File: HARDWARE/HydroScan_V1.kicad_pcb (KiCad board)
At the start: 4 copper layers, 202 x 100 mm, 0 parts

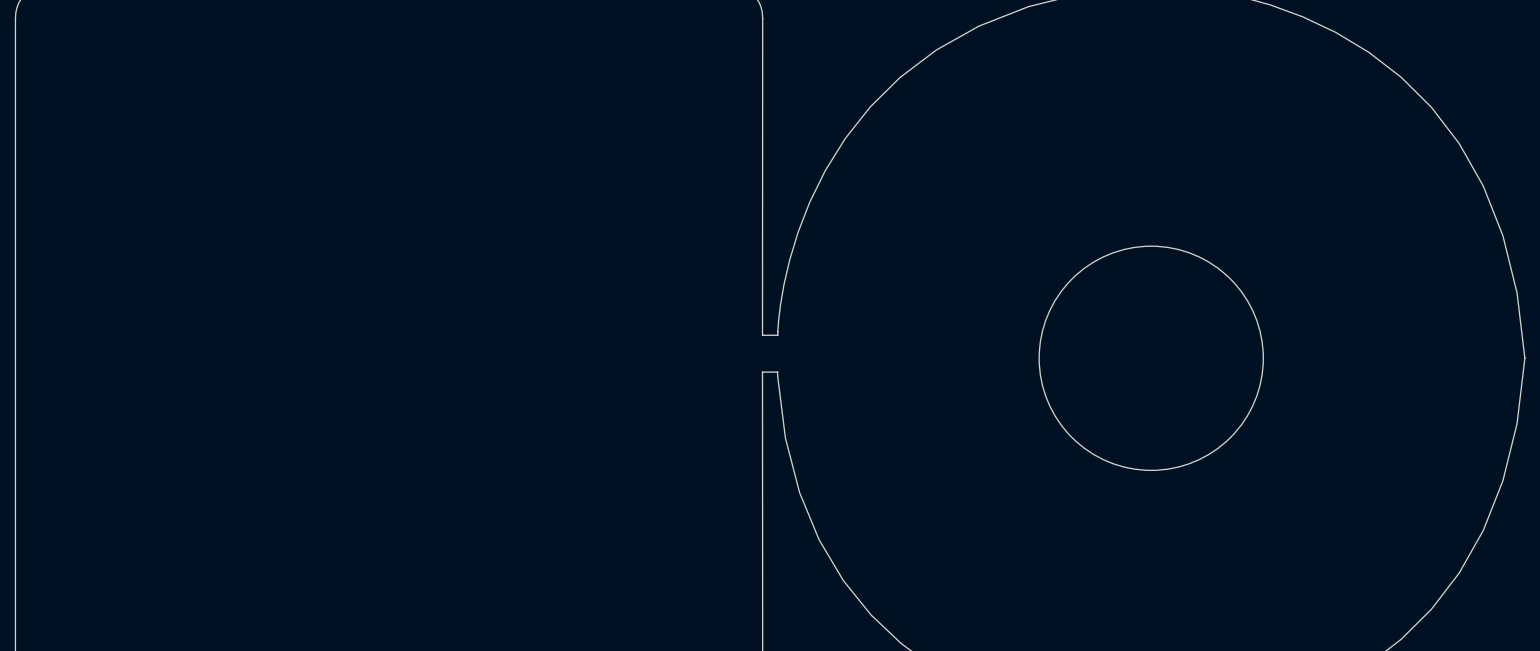
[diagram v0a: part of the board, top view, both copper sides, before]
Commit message: Integrate ESP32
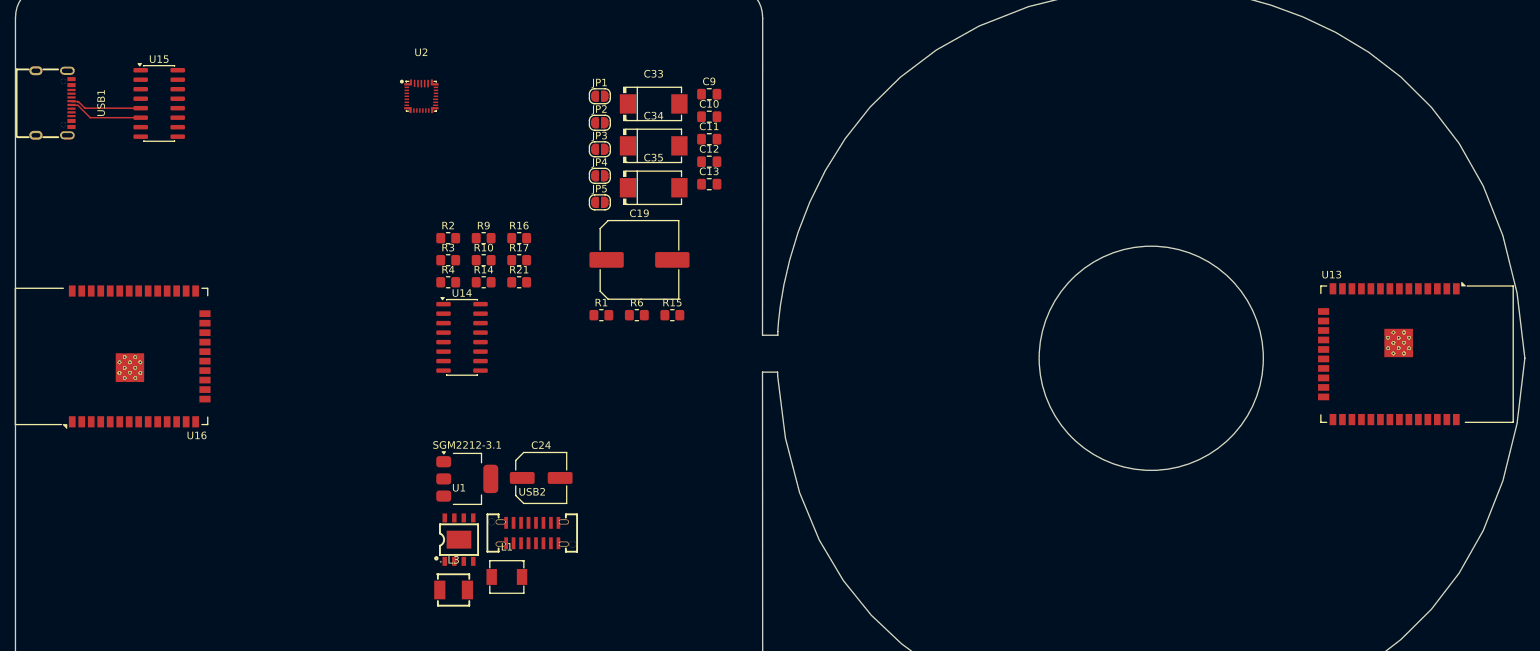
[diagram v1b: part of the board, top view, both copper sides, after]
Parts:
- added C10: 22uf, Capacitor_SMD:C_0805_2012Metric_Pad1.18x1.45mm_HandSolder, F.Cu at (172.8, 137.7)
- added C11: 10uf, Capacitor_SMD:C_0805_2012Metric_Pad1.18x1.45mm_HandSolder, F.Cu at (172.8, 140.7)
- added C12: 22uf, Capacitor_SMD:C_0805_2012Metric_Pad1.18x1.45mm_HandSolder, F.Cu at (172.8, 143.7)
- added C13: 22uf, Capacitor_SMD:C_0805_2012Metric_Pad1.18x1.45mm_HandSolder, F.Cu at (172.8, 146.7)
- added C19: 470uf, Capacitor_SMD:C_Elec_10x10.2, F.Cu at (163.5, 156.8)
- added C24: 47uf, Capacitor_SMD:C_Elec_6.3x7.7, F.Cu at (150.4, 186.0)
- added C33: 25TQC33MYF, EasyEDA:CAP-SMD_L7.3-W4.3-FD, F.Cu at (165.4, 136.0)
- added C34: 25TQC33MYF, EasyEDA:CAP-SMD_L7.3-W4.3-FD, F.Cu at (165.4, 141.6)
- added C35: 25TQC33MYF, EasyEDA:CAP-SMD_L7.3-W4.3-FD, F.Cu at (165.4, 147.2)
- added C9: 10uf, Capacitor_SMD:C_0805_2012Metric_Pad1.18x1.45mm_HandSolder, F.Cu at (172.8, 134.7)
- added JP1: SolderJumper_2_Open, Jumper:SolderJumper-2_P1.3mm_Open_RoundedPad1.0x1.5mm, F.Cu at (158.2, 134.9)
- added JP2: SolderJumper_2_Open, Jumper:SolderJumper-2_P1.3mm_Open_RoundedPad1.0x1.5mm, F.Cu at (158.2, 138.5)
- added JP3: SolderJumper_2_Open, Jumper:SolderJumper-2_P1.3mm_Open_RoundedPad1.0x1.5mm, F.Cu at (158.2, 142.0)
- added JP4: SolderJumper_2_Open, Jumper:SolderJumper-2_P1.3mm_Open_RoundedPad1.0x1.5mm, F.Cu at (158.2, 145.6)
- added JP5: SolderJumper_2_Open, Jumper:SolderJumper-2_P1.3mm_Open_RoundedPad1.0x1.5mm, F.Cu at (158.2, 149.1)
- added L1: APH0420T1R0M, EasyEDA:IND-SMD_L4.4-W4.2, F.Cu at (145.8, 199.3)
- added L3: 0420CDMCCDS-1R0MC, EasyEDA:IND-SMD_L4.2-W4.2_MCW-0420, F.Cu at (138.6, 201.0)
- added R1: 2R, Resistor_SMD:R_0805_2012Metric_Pad1.20x1.40mm_HandSolder, F.Cu at (158.4, 164.2)
- added R10: 0.5R, Resistor_SMD:R_0805_2012Metric_Pad1.20x1.40mm_HandSolder, F.Cu at (142.7, 156.9)
- added R14: 2.2k, Resistor_SMD:R_0805_2012Metric_Pad1.20x1.40mm_HandSolder, F.Cu at (142.7, 159.8)
- added R15: 2.2k, Resistor_SMD:R_0805_2012Metric_Pad1.20x1.40mm_HandSolder, F.Cu at (167.9, 164.2)
- added R16: 2.2k, Resistor_SMD:R_0805_2012Metric_Pad1.20x1.40mm_HandSolder, F.Cu at (147.4, 153.9)
- added R17: 2.2k, Resistor_SMD:R_0805_2012Metric_Pad1.20x1.40mm_HandSolder, F.Cu at (147.4, 156.9)
- added R2: 51k, Resistor_SMD:R_0805_2012Metric_Pad1.20x1.40mm_HandSolder, F.Cu at (137.9, 153.9)
- added R21: 100, Resistor_SMD:R_0805_2012Metric_Pad1.20x1.40mm_HandSolder, F.Cu at (147.4, 159.8)
- added R3: 100, Resistor_SMD:R_0805_2012Metric_Pad1.20x1.40mm_HandSolder, F.Cu at (137.9, 156.9)
- added R4: 100, Resistor_SMD:R_0805_2012Metric_Pad1.20x1.40mm_HandSolder, F.Cu at (137.9, 159.8)
- added R6: 2.2k, Resistor_SMD:R_0805_2012Metric_Pad1.20x1.40mm_HandSolder, F.Cu at (163.2, 164.2)
- added R9: 1k, Resistor_SMD:R_0805_2012Metric_Pad1.20x1.40mm_HandSolder, F.Cu at (142.7, 153.9)
- added SGM2212-3.1: ~, Package_TO_SOT_SMD:SOT-223, F.Cu at (140.5, 186.1)
- added U1: IP2312-4V35, EasyEDA:ESOP-8_L4.9-W3.9-P1.27-LS6.0-BL-EP, F.Cu at (139.4, 194.3)
- added U13: ESP32-WROOM-32D, RF_Module:ESP32-WROOM-32D, F.Cu at (264.6, 169.4)
- added U14: CH340C, Package_SO:SOIC-16_3.9x9.9mm_P1.27mm, F.Cu at (139.8, 167.2)
- added U15: CH340C, Package_SO:SOIC-16_3.9x9.9mm_P1.27mm, F.Cu at (99.2, 135.9)
- added U16: ESP32-WROOM-32D, RF_Module:ESP32-WROOM-32D, F.Cu at (95.8, 169.8)
- added U2: BQ25798RQMR, EasyEDA:QFN-29_L4.0-W4.0-P0.40-TL-BQ25792RQMR, F.Cu at (134.3, 135.0)
- added USB1: TYPE-C 16PIN 2MD, EasyEDA:USB-C-SMD_TYPE-C-16PIN-2MD-073, F.Cu at (85.1, 135.8)
- added USB2: HX-TYPE-C 16P 180 LT H15.0, EasyEDA:USB-C-SMD_HX-TYPE-C-16P-180-LT-H15.0, F.Cu at (149.2, 193.4)
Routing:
- net /Data-_1: track 0.00 -> 9.98 mm
- net /Data+_1: track 0.00 -> 9.71 mm
- added copper zone on In1.Cu, net GND

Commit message: Aclaracion de avances
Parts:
- moved U2 33.9 mm to (141.8, 168.0)
- moved C19 17.6 mm to (152.0, 170.1)
- moved U1 7.60 mm to (132.2, 191.8)
- moved C24 7.60 mm to (143.2, 183.6)
- moved C33 7.60 mm to (158.2, 133.5)
- moved C34 7.60 mm to (158.2, 139.1)
- moved C35 7.60 mm to (158.2, 144.7)
- moved JP1 7.60 mm to (151.0, 132.5)
- moved JP2 7.60 mm to (151.0, 136.0)
- moved JP3 7.60 mm to (151.0, 139.6)
- moved JP4 7.60 mm to (151.0, 143.1)
- moved JP5 7.60 mm to (151.0, 146.7)
- moved L3 7.60 mm to (131.4, 198.5)
- moved R1 7.60 mm to (151.2, 161.8)
- moved R10 7.60 mm to (135.5, 154.4)
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
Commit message: Avances puerto USB C
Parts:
- added C22: 0.1uf, Capacitor_SMD:C_0805_2012Metric_Pad1.18x1.45mm_HandSolder, F.Cu at (175.3, 142.9)
- added C23: 0.1uf, Capacitor_SMD:C_0805_2012Metric_Pad1.18x1.45mm_HandSolder, F.Cu at (175.3, 160.5)
- added D1: SM05.TCT, EasyEDA:SOT-23-3_L2.9-W1.3-P0.95-LS2.4-BR, F.Cu at (169.2, 154.6)
- added D27: LESD5D5.0CT1G, EasyEDA:SOD-523_L1.2-W0.8-LS1.6-BI, F.Cu at (145.9, 152.9)
- added D28: LESD5D5.0CT1G, EasyEDA:SOD-523_L1.2-W0.8-LS1.6-BI, F.Cu at (145.9, 155.1)
- added D29: LESD5D5.0CT1G, EasyEDA:SOD-523_L1.2-W0.8-LS1.6-BI, F.Cu at (145.9, 157.2)
- added D30: LESD5D5.0CT1G, EasyEDA:SOD-523_L1.2-W0.8-LS1.6-BI, F.Cu at (145.9, 159.3)
- added D31: LESD5D5.0CT1G, EasyEDA:SOD-523_L1.2-W0.8-LS1.6-BI, F.Cu at (145.9, 161.5)
- added D33: LESD5D5.0CT1G, EasyEDA:SOD-523_L1.2-W0.8-LS1.6-BI, F.Cu at (145.9, 163.6)
- added D4: SM05.TCT, EasyEDA:SOT-23-3_L2.9-W1.3-P0.95-LS2.4-BR, F.Cu at (169.5, 148.9)
- added R84: 1M, Capacitor_SMD:C_0805_2012Metric_Pad1.18x1.45mm_HandSolder, F.Cu at (175.3, 144.9)
- added R85: 1M, Capacitor_SMD:C_0805_2012Metric_Pad1.18x1.45mm_HandSolder, F.Cu at (175.3, 158.4)
- moved C24 122.2 mm to (164.8, 63.2)
- moved R14 122.2 mm to (157.1, 37.0)
- moved R21 122.2 mm to (161.8, 37.0)
- moved R4 122.2 mm to (152.3, 37.0)
- moved SGM2212-3.1 122.2 mm to (154.8, 63.4)
- moved U14 122.2 mm to (154.2, 44.4)
- moved C11 122.2 mm to (194.4, 20.4)
- moved C33 122.2 mm to (179.8, 13.2)
- moved C35 122.2 mm to (179.8, 24.4)
- moved JP1 122.2 mm to (172.6, 12.1)
- moved JP4 122.2 mm to (172.6, 22.8)
- moved L1 122.2 mm to (160.2, 76.5)
- moved R16 122.2 mm to (161.8, 31.1)
- moved R2 122.2 mm to (152.3, 31.1)
- moved R9 122.2 mm to (157.1, 31.1)
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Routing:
- net /V5_1: track 0.00 -> 12.8 mm
- net Net-(C22-Pad1): track 0.00 -> 9.76 mm, vias 0 -> 1
- net Net-(C23-Pad1): track 0.00 -> 9.12 mm, vias 0 -> 1
- net GND: track 0.00 -> 5.07 mm, vias 0 -> 7
- net /Data+_1: track 9.71 -> 14.7 mm
- net /Data-_1: track 9.98 -> 14.6 mm, vias 0 -> 2
- net /CC1_1: track 0.00 -> 3.02 mm
- net /CC2_1: track 0.00 -> 2.01 mm

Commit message: Avances v1
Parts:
- removed D33: LESD5D5.0CT1G, EasyEDA:SOD-523_L1.2-W0.8-LS1.6-BI
- added D22: 1N5819HW-7-F, EasyEDA:SOD-123_L2.7-W1.6-LS3.7-RD, F.Cu at (179.8, 67.8)
- added D5: SS54_C22452, EasyEDA:SMA_L4.4-W2.8-LS5.4-R-RD, F.Cu at (169.8, 162.6)
- added R13: 5.11k, Capacitor_SMD:C_0805_2012Metric_Pad1.18x1.45mm_HandSolder, F.Cu at (169.8, 145.4)
- added R83: 5.11k, Capacitor_SMD:C_0805_2012Metric_Pad1.18x1.45mm_HandSolder, F.Cu at (169.8, 157.6)
- moved D27 121.6 mm to (206.8, 47.7)
- moved D29 121.6 mm to (206.8, 52.0)
- moved D30 121.6 mm to (206.8, 54.1)
- moved D31 121.6 mm to (206.8, 56.2)
- moved D28 121.6 mm to (206.8, 49.9)
- moved U2 1.58 mm to (161.8, 177.7)
- moved D4 0.90 mm to (169.0, 148.2)
- moved D1 0.30 mm to (169.0, 154.4)
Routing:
- net /V5_1: track 12.8 -> 21.8 mm, vias 0 -> 20
- net GND: track 5.07 -> 11.8 mm, vias 7 -> 34
- net /CC2_1: track 2.01 -> 8.42 mm
- net /CC1_1: track 3.02 -> 8.38 mm
- added copper zone on In2.Cu, net /V5_1
- added copper zone on B.Cu, net GND
- added copper zone on F.Cu, net GND

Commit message: EsP32 terminate
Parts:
- added BOOT1: BOOT, EasyEDA:SW-SMD_4P-L6.0-W6.0-P4.50-LS8.2, F.Cu at (191.2, 85.1)
- added C1: 10uf_25v, Capacitor_SMD:C_0805_2012Metric_Pad1.18x1.45mm_HandSolder, F.Cu at (214.0, 87.8)
- added C14: 0.1uf, Capacitor_SMD:C_0805_2012Metric_Pad1.18x1.45mm_HandSolder, F.Cu at (126.1, 149.3)
- added C15: 0.1uf, Capacitor_SMD:C_0805_2012Metric_Pad1.18x1.45mm_HandSolder, F.Cu at (139.1, 149.3)
- added C16: 100nf, Capacitor_SMD:C_0805_2012Metric_Pad1.18x1.45mm_HandSolder, F.Cu at (118.3, 129.0)
- added C17: 10uf_25v, Capacitor_SMD:C_0805_2012Metric_Pad1.18x1.45mm_HandSolder, F.Cu at (118.3, 131.0)
- added C18: 100nf, Capacitor_SMD:C_0805_2012Metric_Pad1.18x1.45mm_HandSolder, F.Cu at (166.0, 160.0)
- added C2: 0.1uf_50v, Capacitor_SMD:C_0805_2012Metric_Pad1.18x1.45mm_HandSolder, F.Cu at (214.0, 90.9)
- added C20: 0.1uf, Capacitor_SMD:C_0805_2012Metric_Pad1.18x1.45mm_HandSolder, F.Cu at (136.3, 182.5)
- added C21: 10uf, Capacitor_SMD:C_0805_2012Metric_Pad1.18x1.45mm_HandSolder, F.Cu at (223.6, 93.9)
- added C27: 47nf, Capacitor_SMD:C_0805_2012Metric, B.Cu at (146.2, 186.2)
- added C28: 47nf, Capacitor_SMD:C_0805_2012Metric, B.Cu at (149.4, 186.2)
- added C3: 0.1uf_50v, Capacitor_SMD:C_0805_2012Metric_Pad1.18x1.45mm_HandSolder, F.Cu at (214.0, 93.9)
- added C39: 100nf, Capacitor_SMD:C_0805_2012Metric_Pad1.18x1.45mm_HandSolder, F.Cu at (164.0, 137.8)
- added C4: 10uf_25v, Capacitor_SMD:C_0805_2012Metric_Pad1.18x1.45mm_HandSolder, F.Cu at (214.0, 96.9)
- added C40: 100nf, Capacitor_SMD:C_0805_2012Metric_Pad1.18x1.45mm_HandSolder, F.Cu at (154.8, 143.4)
- added C5: 100nf, Capacitor_SMD:C_0805_2012Metric_Pad1.18x1.45mm_HandSolder, F.Cu at (214.0, 99.9)
- added C51: CL32B106KBJNNNE, EasyEDA:C1210, F.Cu at (130.3, 183.1)
- added C52: CL32B106KBJNNNE, EasyEDA:C1210, F.Cu at (133.6, 183.1)
- added C6: 10uf_25v, Capacitor_SMD:C_0805_2012Metric_Pad1.18x1.45mm_HandSolder, F.Cu at (218.8, 87.8)
- added C7: 0.1uf, Capacitor_SMD:C_0805_2012Metric_Pad1.18x1.45mm_HandSolder, F.Cu at (218.8, 90.9)
- added C8: 0.1uf, Capacitor_SMD:C_0805_2012Metric_Pad1.18x1.45mm_HandSolder, F.Cu at (218.8, 93.9)
- added CN2: DB128V-5.08-2P-GN-S, EasyEDA:CONN-TH_2P-P5.08_DIBO_DB128V-5.08, F.Cu at (161.0, 214.1)
- added L2: PSPMAA0805-101M-ANP, EasyEDA:IND-SMD_L8.5-W8.0_PCC-M0854M, F.Cu at (168.6, 153.7)
- added LED10: YLED0805G, EasyEDA:LED0805-FD-GREEN, F.Cu at (232.0, 94.9)
- added LED11: YLED0805G, EasyEDA:LED0805-FD-GREEN, F.Cu at (232.0, 98.2)
- added LED12: YLED0805G, EasyEDA:LED0805-FD-GREEN, F.Cu at (232.0, 101.5)
- added LED13: YLED0805G, EasyEDA:LED0805-FD-GREEN, F.Cu at (232.0, 104.8)
- added LED14: YLED0805G, EasyEDA:LED0805-FD-GREEN, F.Cu at (232.0, 108.1)
- added LED15: YLED0805G, EasyEDA:LED0805-FD-GREEN, F.Cu at (232.0, 111.4)
- added LED16: YLED0805G, EasyEDA:LED0805-FD-GREEN, F.Cu at (175.7, 146.6)
- added LED17: YLED0805G, EasyEDA:LED0805-FD-GREEN, F.Cu at (175.6, 149.0)
- added LED9: YLED0805G, EasyEDA:LED0805-FD-GREEN, F.Cu at (232.0, 91.6)
- added Q13: 2n3904S-RTK/PS_C18536, EasyEDA:SOT-23-3_L2.9-W1.3-P1.90-LS2.4-TR, F.Cu at (174.9, 115.7)
- added Q14: 2n3904S-RTK/PS_C18536, EasyEDA:SOT-23-3_L2.9-W1.3-P1.90-LS2.4-TR, F.Cu at (146.1, 138.1)
- added Q15: 2n3904S-RTK/PS_C18536, EasyEDA:SOT-23-3_L2.9-W1.3-P1.90-LS2.4-TR, F.Cu at (175.5, 98.8)
- added Q16: 2n3904S-RTK/PS_C18536, EasyEDA:SOT-23-3_L2.9-W1.3-P1.90-LS2.4-TR, F.Cu at (146.1, 144.4)
- added R11: 10k, Resistor_SMD:R_0805_2012Metric_Pad1.20x1.40mm_HandSolder, F.Cu at (122.2, 149.3)
- added R12: 10k, Resistor_SMD:R_0805_2012Metric_Pad1.20x1.40mm_HandSolder, F.Cu at (135.3, 149.3)
- added R18: 2.2k, Resistor_SMD:R_0805_2012Metric_Pad1.20x1.40mm_HandSolder, F.Cu at (171.3, 144.1)
- added R22: 2.2k, Resistor_SMD:R_0805_2012Metric_Pad1.20x1.40mm_HandSolder, F.Cu at (171.3, 146.5)
- added R74: 1k, Resistor_SMD:R_0805_2012Metric_Pad1.20x1.40mm_HandSolder, F.Cu at (178.1, 94.3)
- added R75: 1k, Resistor_SMD:R_0805_2012Metric_Pad1.20x1.40mm_HandSolder, F.Cu at (174.6, 94.2)
- added R79: 1k, Resistor_SMD:R_0805_2012Metric_Pad1.20x1.40mm_HandSolder, F.Cu at (150.2, 141.8)
- added R80: 1k, Resistor_SMD:R_0805_2012Metric_Pad1.20x1.40mm_HandSolder, F.Cu at (150.2, 138.9)
- added R81: 0, Resistor_SMD:R_0805_2012Metric_Pad1.20x1.40mm_HandSolder, F.Cu at (144.1, 132.9)
- added R82: 0, Resistor_SMD:R_0805_2012Metric_Pad1.20x1.40mm_HandSolder, F.Cu at (144.1, 131.0)
- added RESET1: RESET, EasyEDA:SW-SMD_4P-L6.0-W6.0-P4.50-LS8.2, F.Cu at (191.2, 92.4)
- added SW2: BOOT, EasyEDA:SW-SMD_4P-L6.0-W6.0-P4.50-LS8.2, F.Cu at (137.1, 153.9)
- added SW4: RESET, EasyEDA:SW-SMD_4P-L6.0-W6.0-P4.50-LS8.2, F.Cu at (124.2, 153.8)
- added U2: L298N, EasyEDA:L298N-module-43x43mm, F.Cu at (103.5, 159.7)
- added U7: LM2576HVS-3.3, EasyEDA:PG-TO-263-5_L10.2-W8.7-P1.70-LS14.4-BR, F.Cu at (156.9, 155.9)
- D5: value SS54_C22452 -> B330A; footprint EasyEDA:SMA_L4.4-W2.8-LS5.4-R-RD -> EasyEDA:SMA_L4.3-W2.6-LS5.1-RD
- R84, R85: footprint Capacitor_SMD:C_0805_2012Metric_Pad1.18x1.45mm_HandSolder -> Resistor_SMD:R_0805_2012Metric_Pad1.20x1.40mm_HandSolder
- U16: footprint RF_Module:ESP32-WROOM-32D -> RF_Module:ESP32-WROOM-32U
- moved C19 117.8 mm to (166.3, 167.4)
- moved L3 99.7 mm to (147.7, 177.7), turned to 180 degrees
- moved C24 83.4 mm to (161.1, 146.6), turned to 180 degrees
- moved U16 25.5 mm to (130.0, 136.0)
- moved U2 16.8 mm to (147.8, 187.1)
- moved C23 16.4 mm to (175.3, 144.1)
- moved D1 16.4 mm to (168.9, 138.0)
- moved R83 16.4 mm to (169.7, 141.2)
- moved U15 16.4 mm to (158.1, 136.4)
- moved USB1 16.4 mm to (174.9, 135.2)
- moved C22 16.4 mm to (175.3, 126.5)
- moved D4 16.4 mm to (168.9, 131.8)
- moved R13 16.4 mm to (169.7, 129.0)
- moved R85 16.4 mm to (175.3, 142.1)
- moved R84 16.4 mm to (175.3, 128.6)
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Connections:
- C19 pad 1: +12V_F -> /SYS
- D5 pad 1: /V5_1 -> Net-(D5-C)
- D5 pad 2: 5V+ -> GND
- U15 pad 16: 3.3V -> /V5_1
- U2 pad 22: /<NO NET> -> unconnected-(U2-BAT-Pad22)
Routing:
- net /EN: track 0.00 -> 51.5 mm, vias 0 -> 2
- net GND: track 11.8 -> 51.3 mm, vias 34 -> 92
- net 3.3V: track 0.00 -> 24.4 mm, vias 0 -> 32
- net Net-(U15-TXD): track 0.00 -> 22.8 mm
- net Net-(U15-RXD): track 0.00 -> 21.9 mm
- net /BOOT: track 0.00 -> 21.0 mm
- net /DTR_1: track 0.00 -> 17.0 mm
- net /RTS_1: track 0.00 -> 12.1 mm
- net Net-(D5-C): track 0.00 -> 10.5 mm
- net /V5_1: track 21.8 -> 15.7 mm, vias 20 -> 13
- net Net-(Q16-B): track 0.00 -> 5.71 mm
- net /TX_1: track 0.00 -> 4.62 mm
- net /RX_1: track 0.00 -> 4.41 mm
- net Net-(Q14-B): track 0.00 -> 3.62 mm
- net Net-(LED17-A): track 0.00 -> 3.47 mm
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- added copper zone on F.Cu, net /SW1
- added copper zone on F.Cu, net /SW2
- added copper zone on F.Cu, net 3.3V
- added copper zone on In2.Cu, net 3.3V
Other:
- board text added: "3V"
- board text added: "5V"
- board text added: "BOOT"
- board text added: "SET"

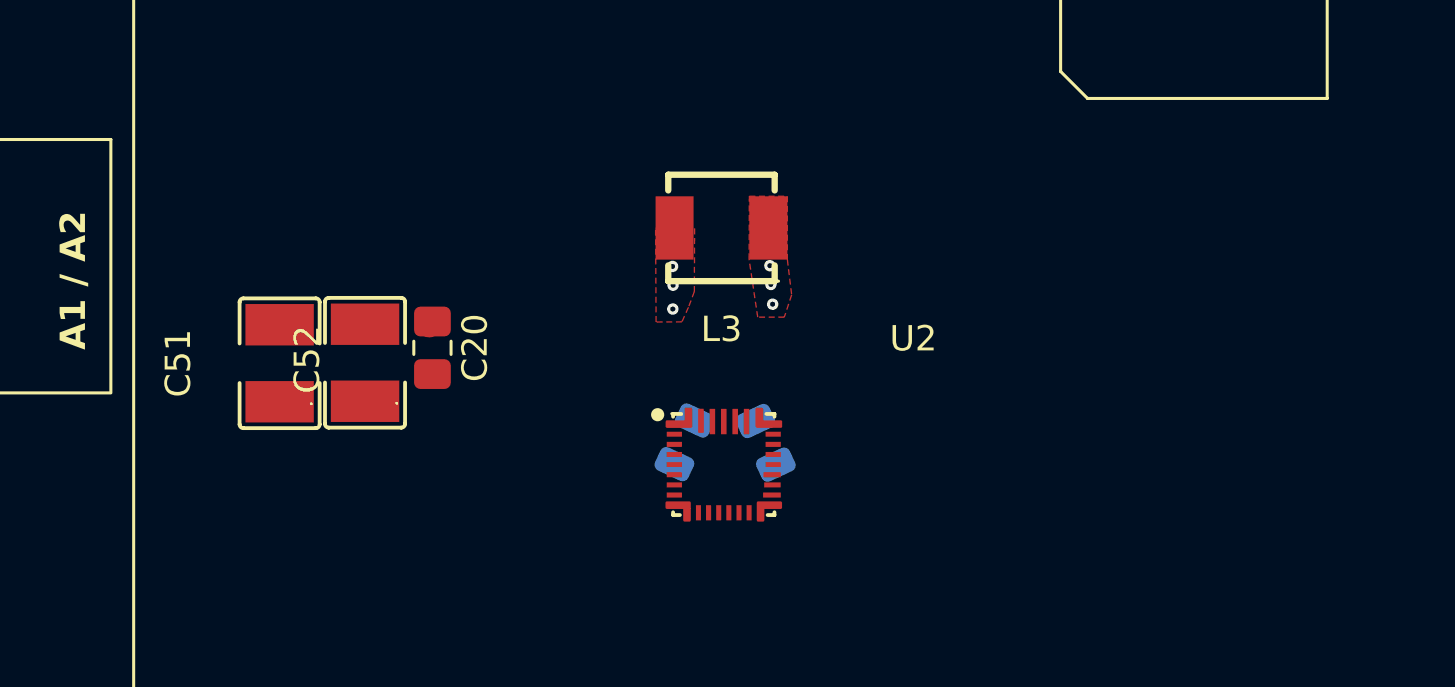
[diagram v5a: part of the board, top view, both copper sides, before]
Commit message: cambios en el fast charging
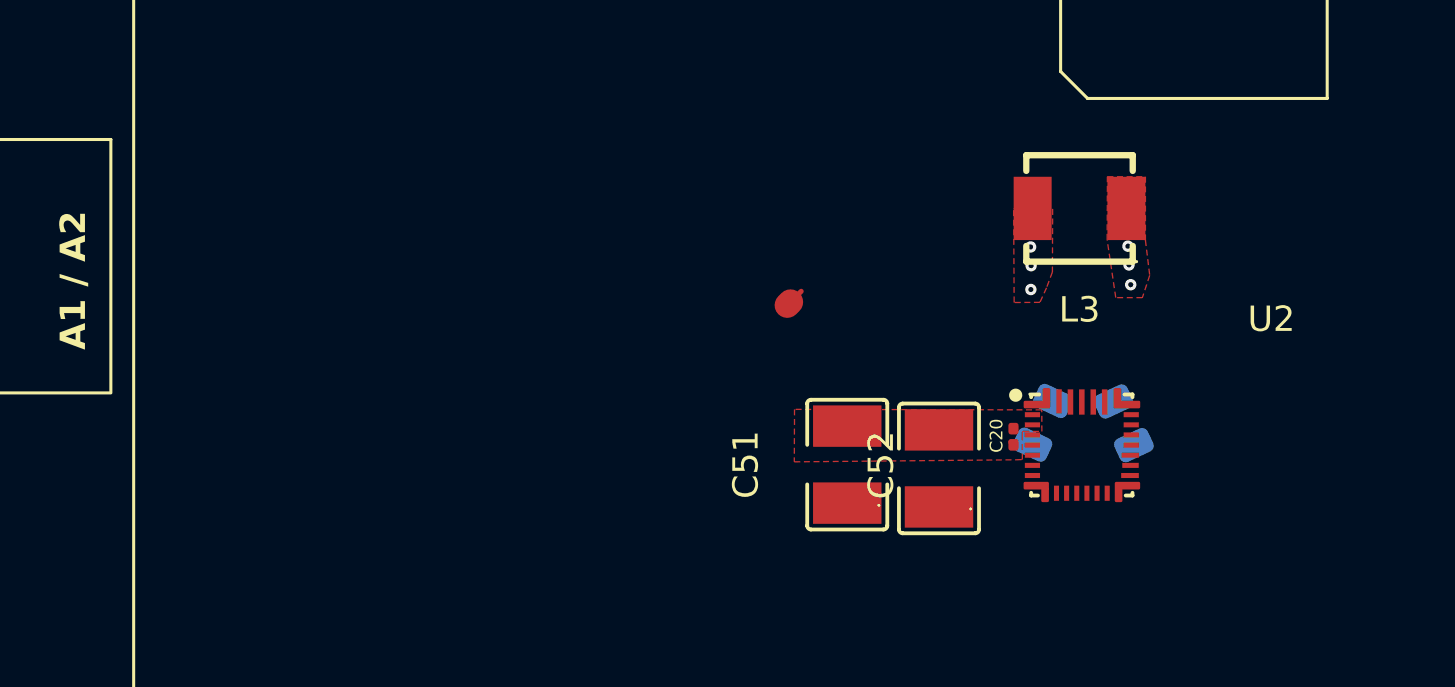
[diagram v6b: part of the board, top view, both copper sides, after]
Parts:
- C20: footprint Capacitor_SMD:C_0805_2012Metric_Pad1.18x1.45mm_HandSolder -> Capacitor_SMD:C_0201_0603Metric
- moved C20 23.2 mm to (159.2, 186.0)
- moved C52 23.0 mm to (156.3, 187.2)
- moved C51 22.8 mm to (152.7, 187.1)
- moved C28 14.2 mm to (163.6, 185.5)
- moved C27 14.2 mm to (160.4, 185.4)
- moved L3 14.2 mm to (161.8, 177.0)
- moved U2 14.2 mm to (161.9, 186.3)
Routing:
- added copper zone on F.Cu, net /VAC1
